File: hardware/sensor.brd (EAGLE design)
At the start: 35.8 x 35.8 mm, 32 parts, among them J1 MICRO_USB_B_HIROSE_ZX62-B-5PA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, J2 DM3AT-SF-PEJM5, SW1 TVAF06-A020B-R, X1 FA-238

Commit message: WIP
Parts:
- removed BOTTOM1, TOP1: P4_2.54, pins:P4_2.54
- removed C27, C28: (no value), rcl:C0402
- removed J2: DM3AT-SF-PEJM5, connector:DM3AT-SF-PEJM5
- removed LED3, LED4: (no value), led:CHIPLED_0603
- removed R10, R9: (no value), rcl:R0402
- removed R11, R12: 1k, rcl:R0402
- added BOTTOM, TOP: P5_2.54, pins:P5_2.54
- added C12, C13: (no value), rcl:C0402
- added CN1, CN2: (no value), jst-ph:S2B-PH-K-S
- added CN3: (no value), jst-ph:B4B-PH-K-S
- added IC1: BN055, BNO055:LGA-28_3.80X5.20/0.5
- added IC2: BME280, bosch-bme280:BME280
- added LED0, LED1: (no value), led:CHIPLED_0603
- added R1, R2, R3, R4: (no value), rcl:R0402
- added R5, R6: 1k, rcl:R0402
- added U$2: P2_2_2.54, pins:P2_2.54
- R7, R8: value (none) -> 22k
- moved R7 21.1 mm to (-5.08, 5.08), turned to 0 degrees
- moved R8 19.7 mm to (5.08, 5.08), turned to 0 degrees
- moved SW1 4.02 mm to (-8.89, -8.89), turned to 0 degrees
- moved X1 2.86 mm to (8.98, -8.90), turned to 270 degrees
- turned C1 to 270 degrees
- turned U2 to 0 degrees
- renumbered C15 to C8, C16 to C9, C17 to C1, C18 to C2, C19 to C3, C20 to C7, C21 to C10, C22 to C11, C23 to C14, C24 to C4, C25 to C5, C26 to C6, FLASH1 to FLASH, U$1 to U2
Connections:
- net I2C_SCL renamed I2C0_SCL
- net SPI0_RX renamed SPI0_MISO
- net SPI0_TX renamed SPI0_MOSI
- net SPI1_RX renamed SPI1_MISO
- net SPI1_TX renamed SPI1_MOSI
- removed net ADC0: RP1.38
- removed net ADC1: RP1.39
- removed net N$10: LED4.A, R10.1
- removed net N$12: R12.1, SW1.P$2
- removed net PWM3_B: RP1.35
- new net GND_IO: IC1.25
- new net N$8: LED0.A, R3.1
- new net SW: R6.1, RP1.35, SW1.P$2
- new net T0: CN2.2, R8.2, RP1.38
- new net T1: CN1.2, R7.2, RP1.39
- new net VDDIO: IC1.28, IC2.6
- net GND: now also BOTTOM.1, BOTTOM.5, C12.2, C13.2, CN3.2, IC1.2, IC2.1, IC2.7, LED0.C, LED1.C, R7.1, R8.1, TOP.1, TOP.5; no longer BOTTOM1.2, C27.2, C28.2, LED3.C, LED4.C, TOP1.2
- net I2C1_SCL: now also CN3.4
- net I2C1_SDA: now also CN3.3
- net LED0: now also R3.2; no longer R9.2
- net LED1: now also R4.2; no longer R10.2
- net N$11: now also C13.1, R5.1; no longer C28.1, R11.1
- net N$9: now also LED1.A, R4.1; no longer LED3.A, R9.1
- net QSPI_SS: now also R6.2; no longer R12.2
- net RX0: now also TOP.4; no longer BOTTOM1.3
- net RX1: now also BOTTOM.4; no longer TOP1.3
- net SWCLK: now also U$2.P$1
- net SWD: now also U$2.P$2
- net TX0: now also TOP.2; no longer BOTTOM1.4
- net TX1: now also BOTTOM.2; no longer TOP1.4
- net USB_DM: now also R1.2; no longer R7.2
- net USB_DM_1: now also R1.1; no longer R7.1
- net USB_DP: now also R2.2; no longer R8.2
- net USB_DP_1: now also R2.1; no longer R8.1
- net V+: now also BOTTOM.3, TOP.3; no longer BOTTOM1.1, TOP1.1
- net VDD: now also CN1.1, CN2.1, CN3.1, IC1.3, IC2.8
- net XIN1: now also C12.1; no longer C27.1
- net XOUT1: now also R5.2; no longer R11.2
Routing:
- net GND: track 57.6 -> 112.9 mm, vias 2 -> 71
- net VDD: track 34.5 -> 73.0 mm, vias 0 -> 6
- net V+: track 23.1 -> 57.0 mm, vias 1 -> 3
- net SWCLK: track 0.00 -> 17.6 mm, vias 0 -> 1
- net SWD: track 0.00 -> 17.1 mm, vias 0 -> 1
- net SW: track 0.00 -> 14.3 mm, vias 0 -> 2
- net TX1: track 12.5 -> 19.8 mm
- net QSPI_SS: track 27.7 -> 22.0 mm
- net LED0: track 12.1 -> 6.55 mm
- net LED1: track 25.3 -> 21.8 mm, vias 0 -> 2
- net XIN1: track 12.9 -> 10.2 mm
- net RX0: track 22.4 -> 20.1 mm
- net N$12: track 1.90 -> 0.00 mm, vias 0 -> 1
- net N$10: track 1.47 -> 0.00 mm
- net N$8: track 0.00 -> 1.41 mm
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- added copper zone on layer 1, net GND
- added copper zone on layer 16, net GND
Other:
- board size 35.8 x 35.8 mm -> 33.5 x 34.6 mm
- board text added: "2022 WASA Rocket"
- board text added: "TERES Module"

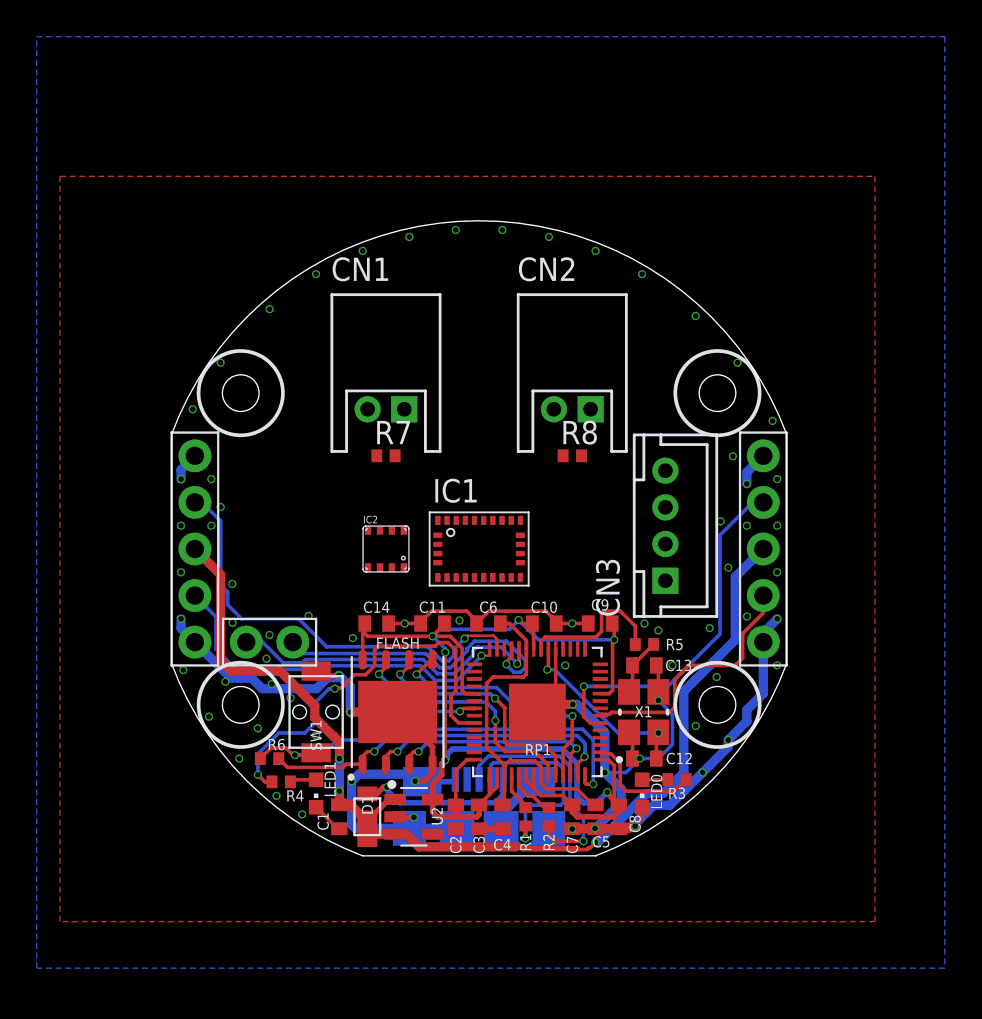
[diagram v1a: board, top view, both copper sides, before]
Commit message: センサーの基盤完了しました。エラー処理とか諸々終わってないので年末年始で頑張ります。抵抗値とかなにも入力してなかったのでしばらくかかりそうです。
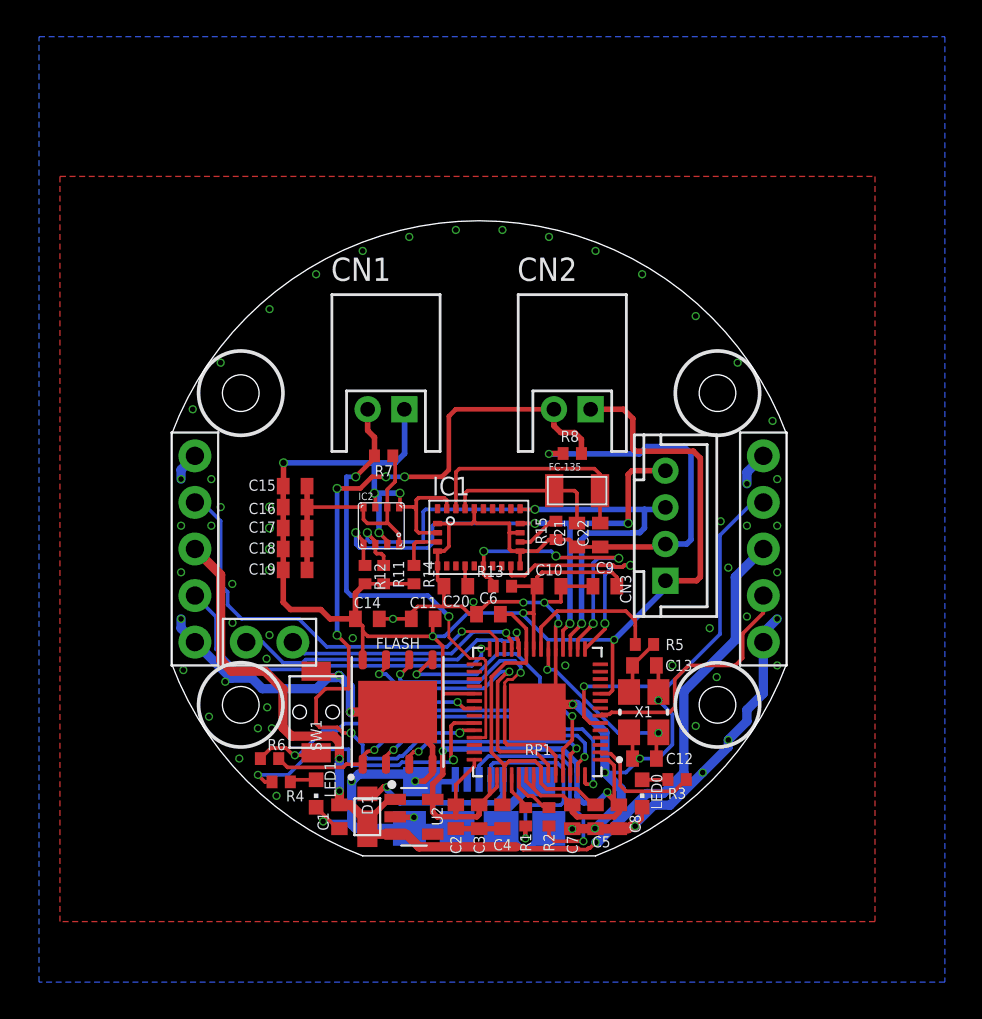
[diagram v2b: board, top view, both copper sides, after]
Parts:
- added C15, C16, C17, C20: 0.1µ, rcl:C0402
- added C18: 6.8n, rcl:C0402
- added C19: 0.12u, rcl:C0402
- added C21, C22: (no value), rcl:C0402
- added FC-135: FC-135, tere:FC-135
- added R11, R12, R13, R14, R15: (no value), rcl:R0402
- moved C10 2.05 mm to (3.81, -2.03)
- moved C9 2.05 mm to (6.86, -2.03)
- moved IC2 1.30 mm to (-5.33, 1.27)
- moved IC1 0.64 mm to (-0.02, 0.64)
- moved C11 0.57 mm to (-3.05, -3.81)
- moved C14 0.57 mm to (-6.10, -3.81)
- moved C6 0.51 mm to (0.51, -3.56)
- moved R7 0.13 mm to (-5.21, 5.08), turned to 180 degrees
- moved R8 0.13 mm to (5.08, 5.21)
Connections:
- removed net GND_IO: IC1.25
- removed net I2C1_SCL: CN3.4, RP1.9
- removed net I2C1_SDA: CN3.3, RP1.8
- removed net SPI1_CS: RP1.16
- removed net SPI1_MISO: RP1.15
- removed net SPI1_MOSI: RP1.18
- removed net SPI1_SCK: RP1.17
- removed net VDDIO: IC1.28, IC2.6
- new net BOOT_LOAD: IC1.4, R14.1
- new net INT: IC1.14, RP1.15
- new net N$1: C20.1, IC1.9
- new net N$10: IC1.17, R15.2
- new net N$15: RP1.26
- new net N$3: C22.2, FC-135.P$2, IC1.27
- new net N$4: C21.2, FC-135.P$1, IC1.26
- new net RESET: IC1.11, R13.1, RP1.16
- net GND: now also C15.2, C16.2, C17.2, C18.2, C19.2, C20.2, C21.1, C22.1, IC1.15, IC1.16, IC1.18, IC1.25, IC1.5, IC1.6, IC2.5, R15.1
- net I2C0_SCL: now also CN3.4, IC1.19, IC2.4, R12.1, RP1.18; no longer RP1.12
- net I2C0_SDA: now also CN3.3, IC1.20, IC2.3, R11.1, RP1.17; no longer RP1.11
- net VDD: now also C15.1, C16.1, C17.1, C18.1, C19.1, IC1.28, IC2.2, IC2.6, R11.2, R12.2, R13.2, R14.2
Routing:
- net VDD: track 73.0 -> 138.6 mm, vias 6 -> 9
- net GND: track 112.9 -> 172.0 mm, vias 71 -> 69
- net T0: track 0.00 -> 43.7 mm, vias 0 -> 6
- net I2C0_SDA: track 0.00 -> 32.5 mm, vias 0 -> 3
- net I2C0_SCL: track 0.00 -> 31.3 mm, vias 0 -> 4
- net T1: track 0.00 -> 25.7 mm, vias 0 -> 2
- net RESET: track 0.00 -> 16.3 mm, vias 0 -> 4
- net INT: track 0.00 -> 13.5 mm, vias 0 -> 2
- net N$3: track 0.00 -> 12.7 mm
- net N$4: track 0.00 -> 8.70 mm
- net LED1: track 21.8 -> 16.3 mm
- net QSPI_SCLK: track 13.6 -> 17.4 mm
- net SWD: track 17.1 -> 13.4 mm
- net QSPI_SD3: track 13.8 -> 17.0 mm
- net BOOT_LOAD: track 0.00 -> 2.50 mm
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
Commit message: べたGND前です。esp32のschはノータッチなのでここに上がってないです。よろしくお願いします。
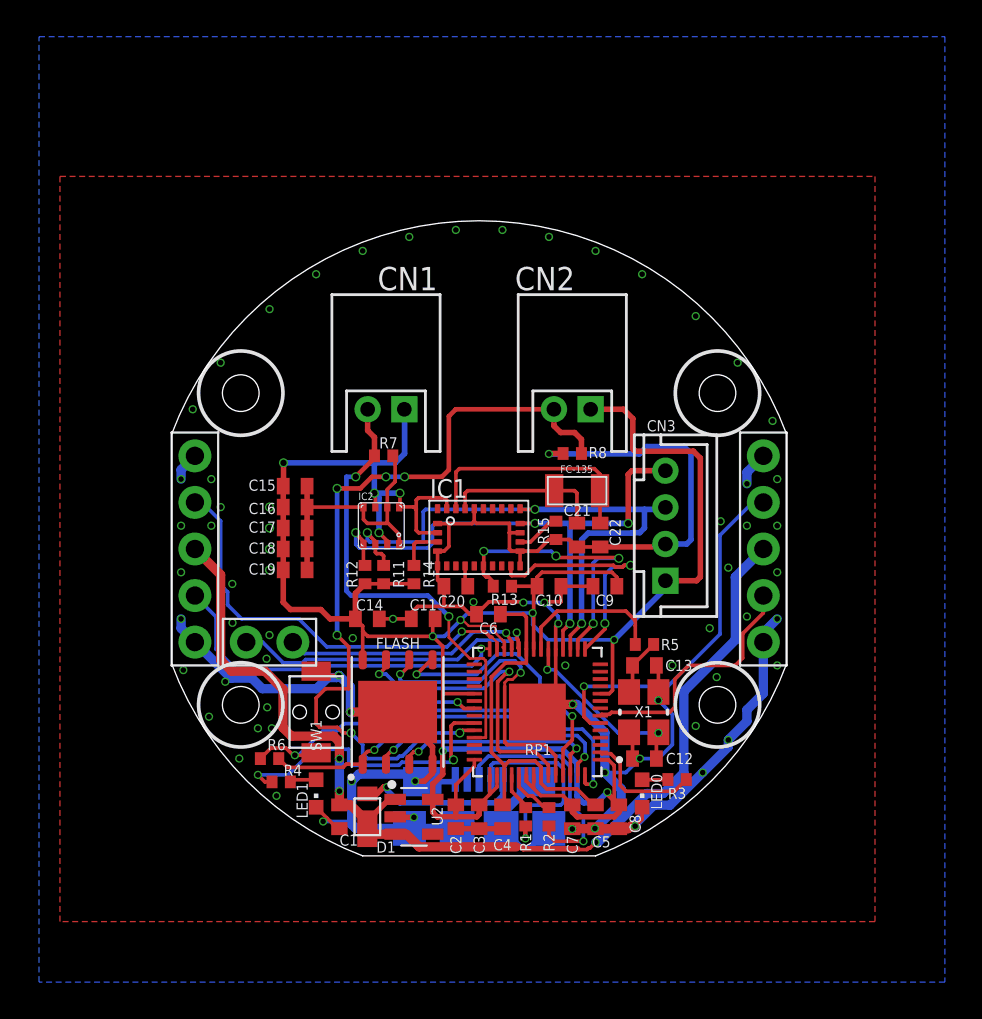
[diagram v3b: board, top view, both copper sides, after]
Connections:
- removed net N$15: RP1.26
- net VDD: now also RP1.26
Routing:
- net VDD: track 138.6 -> 142.0 mm, vias 9 -> 10

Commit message: LiPoのだけできなかったのですが、それ以外のべたGND済のものです。
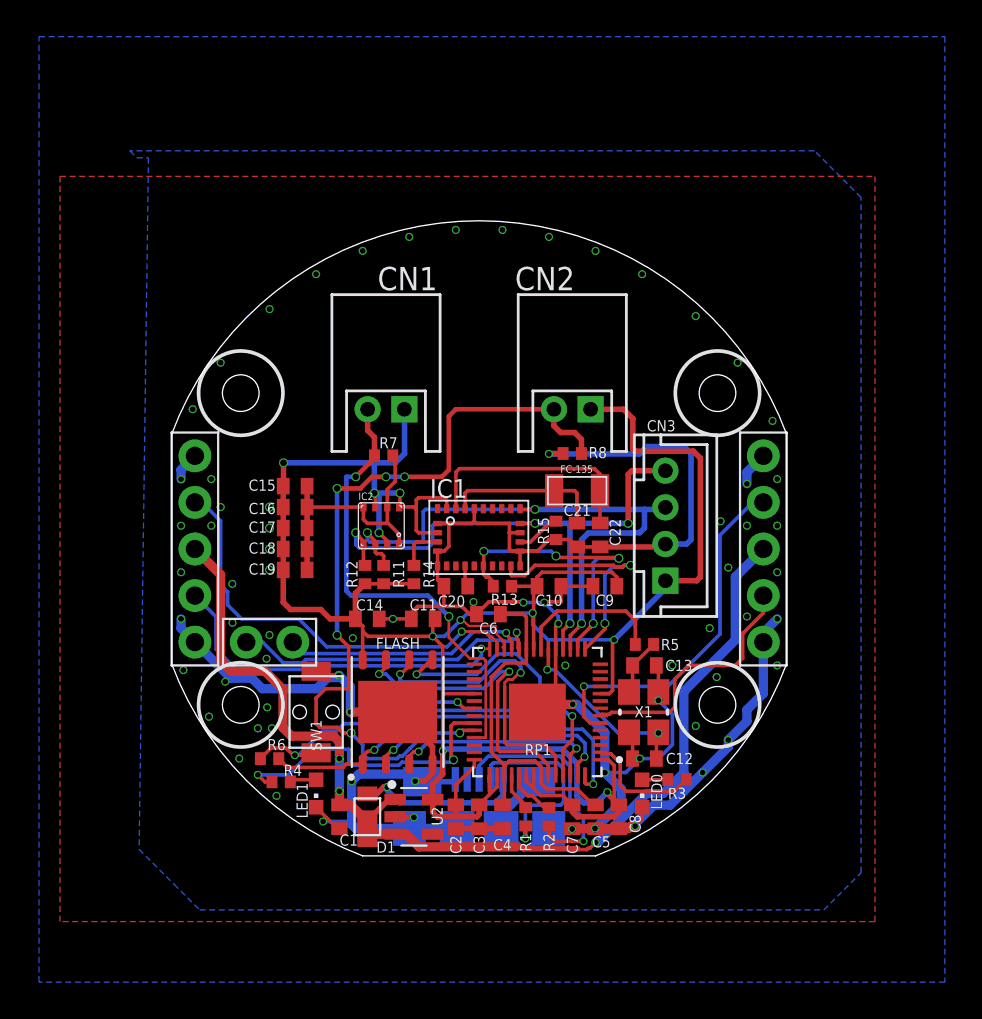
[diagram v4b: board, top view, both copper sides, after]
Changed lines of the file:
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@@
 <wire x1="-7.0795" y1="-14.859" x2="-6.9525" y2="-14.732" width="0.2" layer="16"/>
 <wire x1="-1.27" y1="-15.255" x2="0" y2="-15.255" width="0.3048" layer="1"/>
+<polygon width="0.1524" layer="16">
+<vertex x="-18.542" y="-16.383"/>
+<vertex x="-16.637" y="-18.288"/>
+<vertex x="-15.24" y="-19.685"/>
+<vertex x="18.796" y="-19.685"/>
+<vertex x="20.828" y="-17.653"/>
+<vertex x="20.828" y="19.177"/>
+<vertex x="18.288" y="21.717"/>
+<vertex x="-19.05" y="21.717"/>
+<vertex x="-18.669" y="21.336"/>
+<vertex x="-18.034" y="21.336"/>
+</polygon>
 <wire x1="11.811" y1="12.7" x2="14.097" y2="10.16" width="0" layer="19" extent="1-1"/>
 <wire x1="16.002" y1="6.985" x2="14.097" y2="10.16" width="0" layer="19" extent="1-1"/>

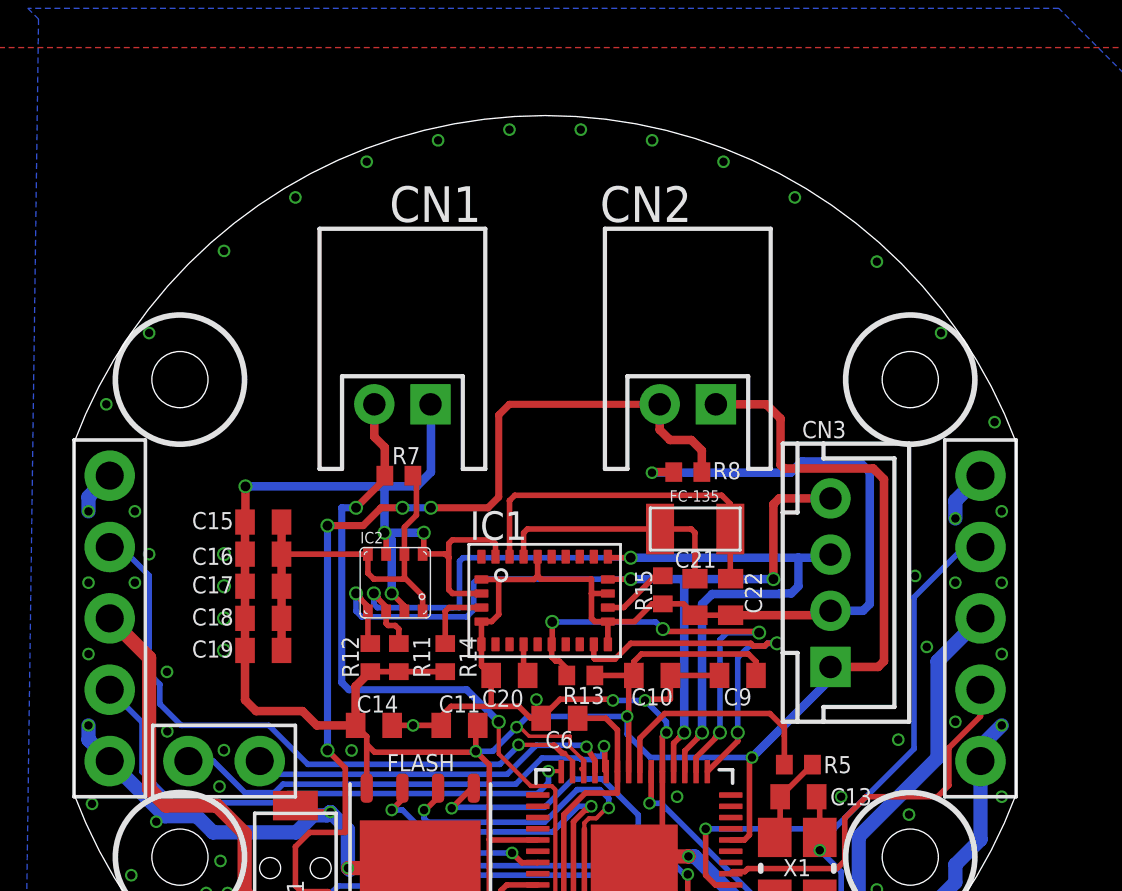
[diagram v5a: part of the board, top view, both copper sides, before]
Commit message: シルクを調整
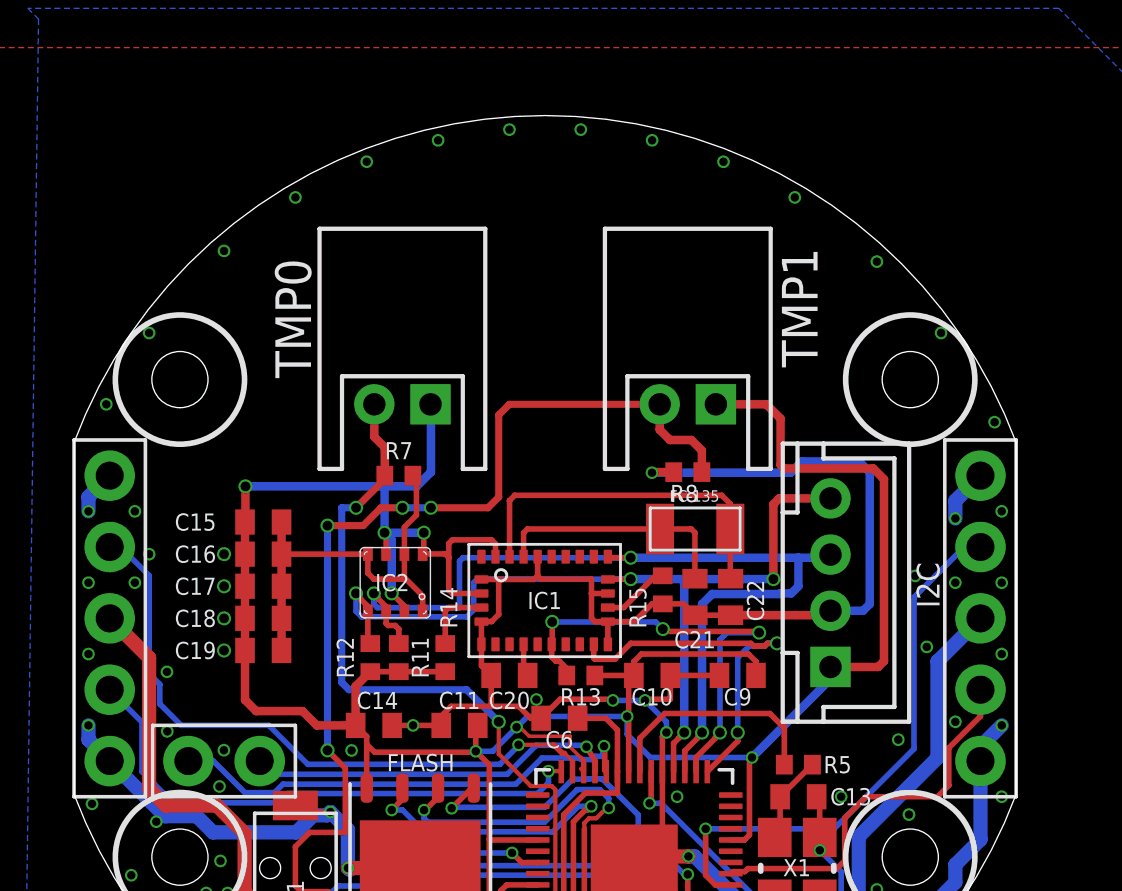
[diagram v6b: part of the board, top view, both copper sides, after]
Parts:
- renumbered CN1 to TMP0, CN2 to TMP1, CN3 to I2C
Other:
- board text added: "TERES Sensor Module"
- board text removed: "TERES Module"
